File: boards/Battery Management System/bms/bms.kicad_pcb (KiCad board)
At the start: 2 copper layers, 23 parts, among them J1 Screw_Terminal_01x05, J2 Screw_Terminal_01x02, J3 Screw_Terminal_01x02, Q1 PMOS, Q2 PMOS, Q3 PMOS, Q4 PMOS, Q5 NMOS, Q6 NMOS, Q7 NMOS, Q8 NMOS, U1 BD48L32G, U2 BD48L32G, U3 BD48L32G, U4 BD48L32G

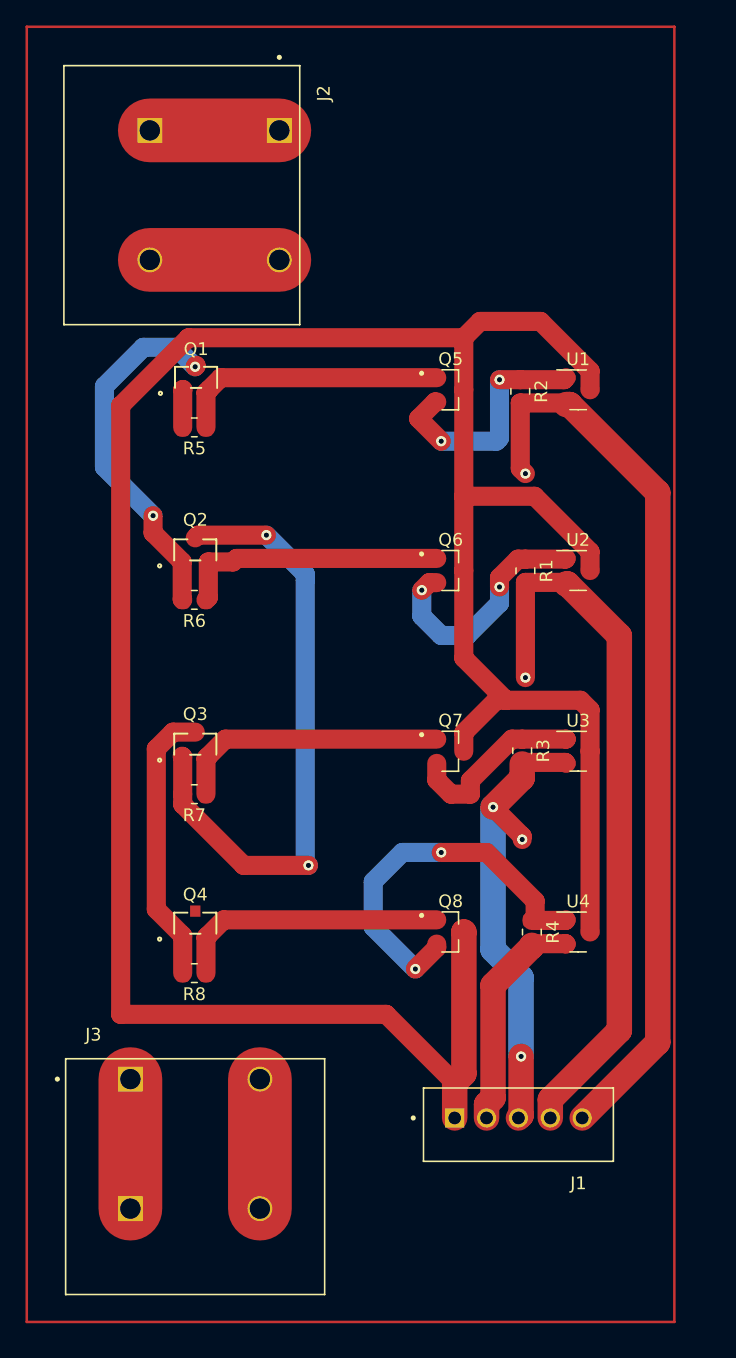
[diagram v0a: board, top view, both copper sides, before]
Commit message: updated bms schematic and layout
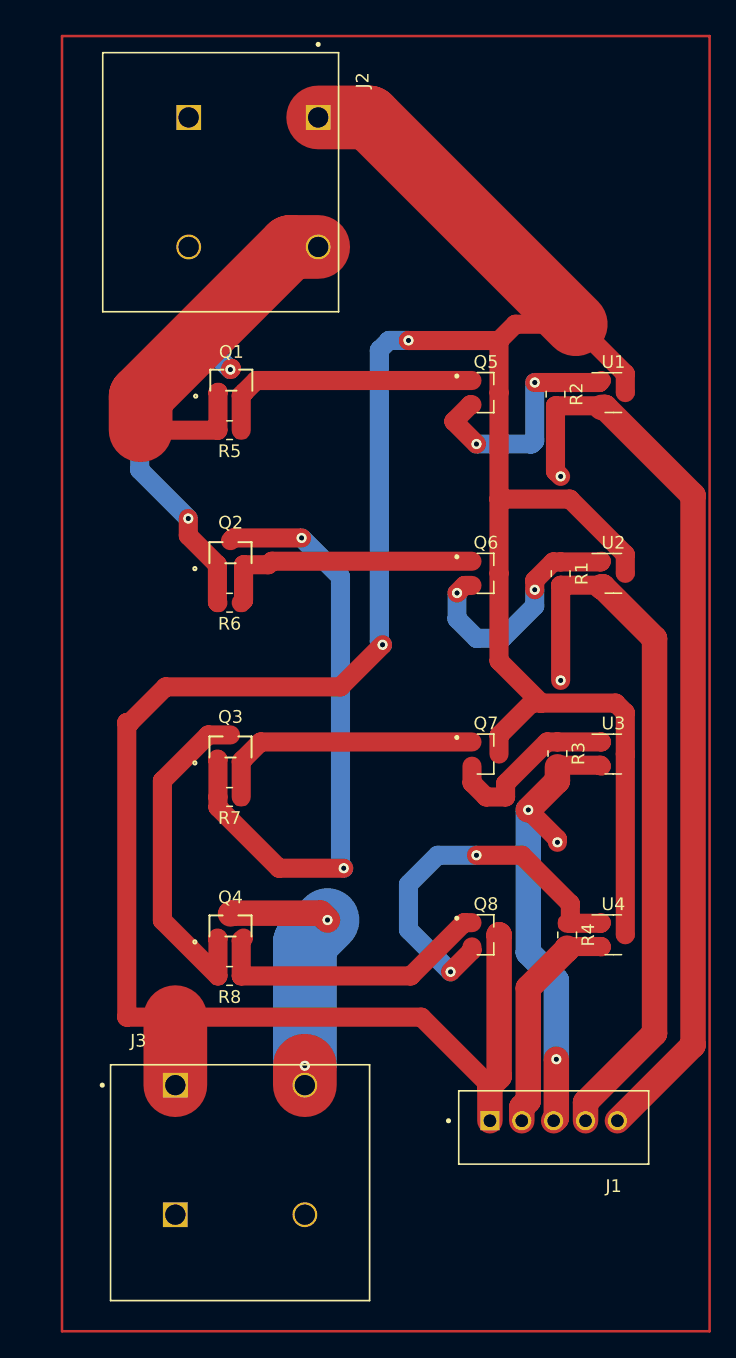
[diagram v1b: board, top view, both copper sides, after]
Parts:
- J2, J3: value Screw_Terminal_01x02 -> 1986660-2
- moved J3 3.56 mm to (102.6, 119.9)
- moved J2 3.21 mm to (113.8, 43.9)
- moved J1 2.77 mm to (132.3, 123.2)
- moved Q1 2.77 mm to (107.0, 64.6)
- moved R1 2.77 mm to (132.8, 79.7)
- moved R2 2.77 mm to (132.4, 65.6)
- moved R5 2.77 mm to (106.8, 68.5)
- moved R6 2.77 mm to (106.8, 82.0)
- moved R7 2.77 mm to (106.8, 97.2)
- moved R8 2.77 mm to (106.8, 111.3)
- moved U1 2.77 mm to (136.9, 65.5)
- moved U2 2.77 mm to (136.9, 79.7)
- moved U3 2.77 mm to (136.9, 93.9)
- moved U4 2.77 mm to (136.9, 108.1)
- moved Q2 2.77 mm to (106.9, 78.1)
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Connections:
- J2 pad 1_1: (no net) -> GND
- J2 pad 2_1: (no net) -> /V_BAT_IN
- J3 pad 1_1: (no net) -> GND
- J3 pad 2_1: (no net) -> /V_BAT_OUT
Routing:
- net (no net): track 40.6 -> 0.00 mm
- net GND: track 206.9 -> 243.2 mm, vias 0 -> 2
- net /V_BAT_IN: track 3.09 -> 30.7 mm
- net /V_BAT_OUT: track 0.00 -> 21.5 mm, vias 0 -> 2
- net Net-(Q3-S): track 22.1 -> 27.0 mm
- net Net-(Q4-G): track 21.7 -> 23.2 mm

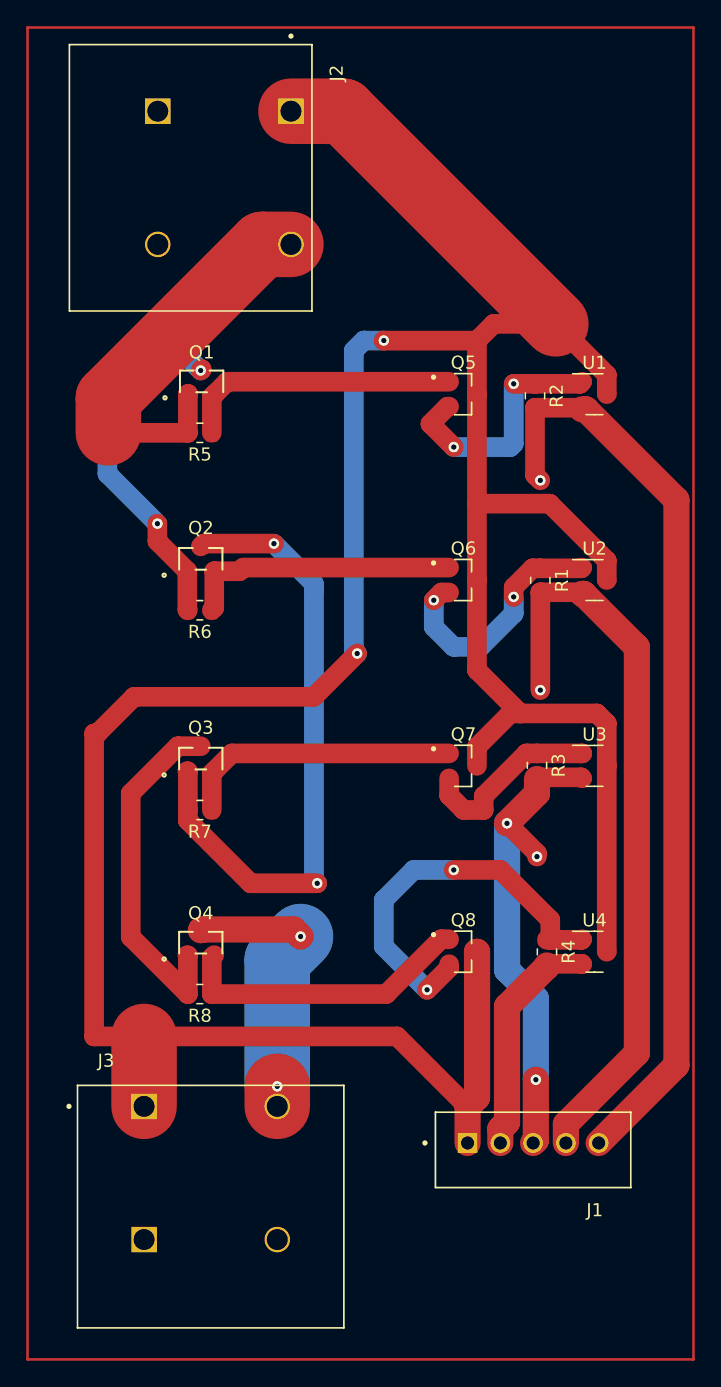
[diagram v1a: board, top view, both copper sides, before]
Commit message: Redid pcb layout and added LEDs.
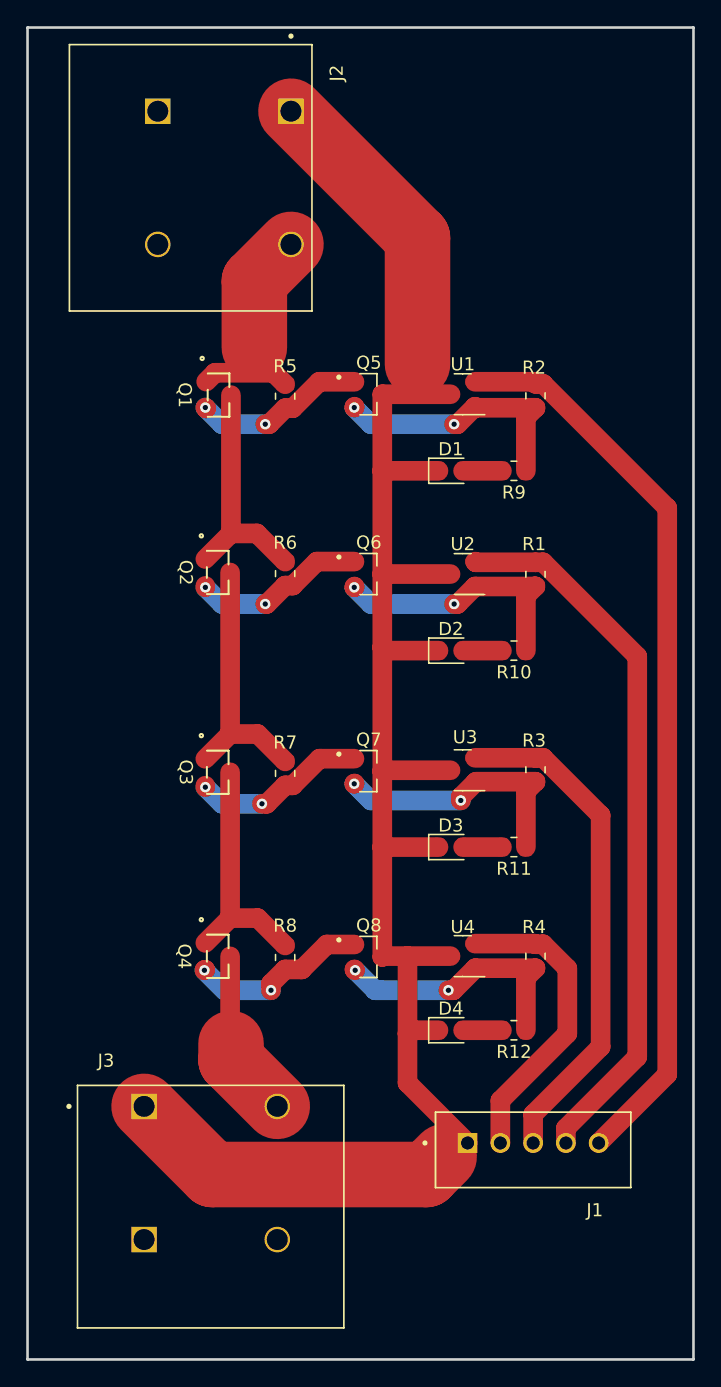
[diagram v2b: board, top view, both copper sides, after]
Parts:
- added D1: LED, LED_SMD:LED_0805_2012Metric, F.Cu at (126.0, 71.4)
- added D2: LED, LED_SMD:LED_0805_2012Metric, F.Cu at (126.0, 85.1)
- added D3: LED, LED_SMD:LED_0805_2012Metric, F.Cu at (126.0, 100.1)
- added D4: LED, LED_SMD:LED_0805_2012Metric, F.Cu at (126.0, 114.0)
- added R10: 6Ω, Resistor_SMD:R_0805_2012Metric, F.Cu at (130.8, 85.1)
- added R11: 6Ω, Resistor_SMD:R_0805_2012Metric, F.Cu at (130.8, 100.1)
- added R12: 6Ω, Resistor_SMD:R_0805_2012Metric, F.Cu at (130.8, 114.0)
- added R9: 6Ω, Resistor_SMD:R_0805_2012Metric, F.Cu at (130.8, 71.4)
- moved U2 10.1 mm to (126.9, 79.2), turned to 180 degrees
- moved U3 10.1 mm to (126.9, 94.2), turned to 180 degrees
- moved U4 10.1 mm to (126.9, 108.4), turned to 180 degrees
- moved U1 10.1 mm to (126.9, 65.5), turned to 180 degrees
- moved Q6 7.23 mm to (119.7, 79.2)
- moved Q7 7.23 mm to (119.7, 94.3)
- moved Q8 7.23 mm to (119.7, 108.5)
- moved Q5 7.22 mm to (119.7, 65.5)
- moved R7 7.08 mm to (113.3, 94.5), turned to 90 degrees
- moved R8 7.08 mm to (113.3, 108.5), turned to 90 degrees
- moved R5 7.08 mm to (113.3, 65.7), turned to 90 degrees
- moved R6 7.08 mm to (113.3, 79.2), turned to 90 degrees
- moved Q1 1.66 mm to (108.3, 65.6), turned to -90 degrees
- moved Q2 1.66 mm to (108.2, 79.1), turned to -90 degrees
- moved Q3 1.66 mm to (108.2, 94.4), turned to -90 degrees
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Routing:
- net GND: track 243.2 -> 144.3 mm, vias 2 -> 0
- net Net-(Q2-S): track 48.6 -> 20.1 mm, vias 2 -> 0
- net /V_BAT_IN: track 30.7 -> 15.7 mm
- net /CON_4: track 30.3 -> 20.2 mm
- net Net-(Q1-S): track 28.5 -> 18.3 mm, vias 2 -> 0
- net Net-(Q4-G): track 23.2 -> 13.9 mm, vias 0 -> 2
- net /V_BAT_OUT: track 21.5 -> 12.9 mm, vias 2 -> 0
- net Net-(Q3-G): track 21.8 -> 13.4 mm, vias 0 -> 2
- net Net-(Q1-G): track 21.7 -> 13.3 mm, vias 0 -> 2
- net Net-(Q3-S): track 27.0 -> 18.9 mm
- net Net-(Q2-G): track 21.1 -> 13.4 mm, vias 0 -> 2
- net /CON_3: track 14.3 -> 20.4 mm, vias 0 -> 2
- net /V_CELL_4: track 17.7 -> 23.3 mm
- net Net-(D4-A): track 0.00 -> 2.96 mm
- net Net-(D3-A): track 0.00 -> 2.96 mm
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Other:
- board outline added: 50.8 x 101.6 mm

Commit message: Worked on schematic and PCB
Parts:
- removed Q1, Q2, Q3, Q4: PMOS, BSS84_7_F:SOT-23_DIO
- removed Q5, Q6, Q7, Q8: NMOS, BSS138:SOT95P240X111-3N
- added K1: HE1AN-W-DC6V-Y6, footprints:HE1AN-W-DC6V_PAN, F.Cu at (163.2, 70.5)
- added K2: HE1AN-W-DC6V-Y6, footprints:HE1AN-W-DC6V_PAN, F.Cu at (200.0, 70.5)
- added K3: HE1AN-W-DC6V-Y6, footprints:HE1AN-W-DC6V_PAN, F.Cu at (236.9, 70.5)
- added K4: HE1AN-W-DC6V-Y6, footprints:HE1AN-W-DC6V_PAN, F.Cu at (273.7, 70.5)
- added R13: 100kΩ, Resistor_SMD:R_0805_2012Metric, F.Cu at (61.4, 82.6)
- added R14: 100kΩ, Resistor_SMD:R_0805_2012Metric, F.Cu at (61.4, 88.5)
- added R15: 100kΩ, Resistor_SMD:R_0805_2012Metric, F.Cu at (61.4, 94.0)
- added R16: 100kΩ, Resistor_SMD:R_0805_2012Metric, F.Cu at (61.4, 96.9)
- added R17: 5kΩ, Resistor_SMD:R_0805_2012Metric, F.Cu at (65.8, 82.6)
- added R18: 10kΩ, Resistor_SMD:R_0805_2012Metric, F.Cu at (65.8, 88.5)
- added R19: 10kΩ, Resistor_SMD:R_0805_2012Metric, F.Cu at (65.8, 94.0)
- added R20: 5kΩ, Resistor_SMD:R_0805_2012Metric, F.Cu at (65.8, 96.9)
- added R21: 10kΩ, Resistor_SMD:R_0805_2012Metric, F.Cu at (70.2, 82.6)
- added R22: 5kΩ, Resistor_SMD:R_0805_2012Metric, F.Cu at (70.2, 88.5)
- added R23: 10kΩ, Resistor_SMD:R_0805_2012Metric, F.Cu at (70.2, 94.0)
- added R24: 5kΩ, Resistor_SMD:R_0805_2012Metric, F.Cu at (70.2, 96.9)
- added U5: Opamp_Quad, footprints:SOT23_DYY_TEX, F.Cu at (62.0, 101.4)
- R10, R11, R12, R9: value 6Ω -> 70Ω
- moved R5 57.1 mm to (157.6, 101.8), turned to 0 degrees
- moved R6 51.1 mm to (157.6, 104.8), turned to 0 degrees
- moved R7 46.2 mm to (157.6, 107.7), turned to 0 degrees
- moved R8 44.3 mm to (157.6, 110.7), turned to 0 degrees
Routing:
- net GND: track 144.3 -> 121.0 mm
- net Net-(Q2-S): track 20.1 -> 0.00 mm
- net Net-(Q3-S): track 18.9 -> 0.00 mm
- net Net-(Q1-S): track 18.3 -> 0.00 mm
- net /V_BAT_IN: track 15.7 -> 0.00 mm
- net Net-(Q4-G): track 13.9 -> 0.00 mm, vias 2 -> 0
- net Net-(Q3-G): track 13.4 -> 0.00 mm, vias 2 -> 0
- net Net-(Q2-G): track 13.4 -> 0.00 mm, vias 2 -> 0
- net Net-(Q1-G): track 13.3 -> 0.00 mm, vias 2 -> 0
- net /V_BAT_OUT: track 12.9 -> 0.00 mm
- net /CON_3: track 20.4 -> 11.7 mm, vias 2 -> 1
- net /CON_2: track 20.2 -> 12.0 mm, vias 2 -> 1
- net /CON_1: track 20.1 -> 11.9 mm, vias 2 -> 1
- net /CON_4: track 20.2 -> 12.4 mm, vias 2 -> 1

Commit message: Edited schematic and PCB
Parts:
- added U5: Opamp_Quad, footprints:SOT23_DBV_5_TEX-L, F.Cu at (48.9, 133.1)
- added U6: 74AUC2G08, footprints:D14-L, F.Cu at (50.4, 125.7)
- added U7: 74AUC2G08, footprints:D14-L, F.Cu at (58.5, 125.7)
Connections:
- K1 pad 1: Net-(K1-Pad1) -> /V_BAT_OUT

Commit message: Edited schematic and PCB
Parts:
- removed K2, K3, K4: HE1AN-W-DC6V-Y6, footprints:HE1AN-W-DC6V_PAN
- removed the R7 at (157.6, 107.7)
- removed the R8 at (157.6, 110.7)
- removed the U5 at (62.0, 101.4)
- removed the U5 at (48.9, 133.1)
- removed U7: 74AUC2G08, footprints:D14-L
- added U5: SN74HC08DR, SN74HC08DR:SOIC127P600X175-14N, F.Cu at (25.5, 108.0)
- K1: footprint footprints:HE1AN-W-DC6V_PAN -> HE1AN_W_DC6V_Y6:HE1AN-W-DC6V_PAN
- R5: value 100kΩ -> 10kΩ
- R6: value 100kΩ -> 5kΩ
- U6: value 74AUC2G08 -> TL071HIDBVR; footprint footprints:D14-L -> TL071HIDBVR:SOT23_DBV_5_TEX-L
- moved R5 103.1 mm to (62.6, 61.7)
- moved R6 103.1 mm to (62.6, 64.7)
- moved U6 65.4 mm to (67.3, 62.5)
- renumbered R2 to R1, R12 to R10, R1 to R2, R9 to R7, R10 to R8, R11 to R9
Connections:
- K1 pad 5: Net-(K1-Pad5) -> Net-(U6-OUT)
- R5 pad 1: Net-(Q1-G) -> GND
- R5 pad 2: /V_BAT_IN -> Net-(U6-IN-)
- R6 pad 1: Net-(Q2-G) -> Net-(U6-IN-)
- R6 pad 2: Net-(Q1-S) -> Net-(U6-OUT)
- U6 pad 1: /CON_1 -> Net-(U6-OUT)
- U6 pad 2: /CON_2 -> GND
- U6 pad 4: (no net) -> Net-(U6-IN-)
- U6 pad 5: Net-(U6-Pad5) -> /V_BAT_IN

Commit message: Updated Schematic and PCB
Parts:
- removed R14, R15, R16: 100kΩ, Resistor_SMD:R_0805_2012Metric
- removed R17, R20, R22, R24: 5kΩ, Resistor_SMD:R_0805_2012Metric
- removed R18, R19, R21, R23: 10kΩ, Resistor_SMD:R_0805_2012Metric
- moved U5 100.3 mm to (117.6, 68.3), turned to 180 degrees
- moved R11 74.6 mm to (127.3, 47.5), turned to -90 degrees
- moved R6 73.3 mm to (133.9, 47.5), turned to 90 degrees
- moved R5 71.7 mm to (133.9, 53.8), turned to 90 degrees
- moved U6 59.6 mm to (126.2, 53.8)
- moved K1 54.1 mm to (122.7, 106.4), turned to 180 degrees
- moved D1 7.76 mm to (132.4, 67.0)
- moved D2 7.76 mm to (132.4, 80.7)
- moved D3 7.76 mm to (132.4, 95.7)
- moved D4 7.76 mm to (132.4, 109.7)
- moved R10 7.76 mm to (137.2, 109.7)
- moved R2 7.76 mm to (138.8, 74.9)
- moved R3 7.76 mm to (138.8, 89.8)
- moved R4 7.76 mm to (138.8, 104.0)
- moved R7 7.76 mm to (137.2, 67.0)
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- renumbered R13 to R11
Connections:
- U5 pad 1: /CON_1 -> /CON_4
- U5 pad 10: Net-(U5-2Y) -> Net-(U5-1Y)
- U5 pad 2: /CON_2 -> /CON_3
- U5 pad 4: /CON_3 -> /CON_2
- U5 pad 5: /CON_4 -> /CON_1
- U5 pad 9: Net-(U5-1Y) -> Net-(U5-2Y)
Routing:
- net /V_BAT_IN: track 0.00 -> 61.8 mm
- net GND: track 121.0 -> 171.9 mm, vias 0 -> 3
- net Net-(U6-OUT): track 0.00 -> 50.9 mm, vias 0 -> 3
- net /CON_4: track 12.4 -> 54.1 mm, vias 1 -> 2
- net /CON_3: track 11.7 -> 41.8 mm, vias 1 -> 2
- net /CON_2: track 12.0 -> 28.6 mm, vias 1 -> 2
- net /V_BAT_OUT: track 0.00 -> 16.5 mm
- net /CON_1: track 11.9 -> 26.3 mm, vias 1 -> 2
- net Net-(U5-3Y): track 0.00 -> 13.9 mm
- net Net-(U6-IN-): track 0.00 -> 12.6 mm, vias 0 -> 2
- net /V_CELL_4: track 23.3 -> 34.1 mm, vias 0 -> 2
- net /V_CELL_2: track 54.7 -> 61.5 mm, vias 0 -> 2
- net Net-(U5-1Y): track 0.00 -> 6.45 mm
- net /V_CELL_3: track 38.5 -> 44.6 mm
- net Net-(U5-2Y): track 0.00 -> 4.95 mm
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
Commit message: Updated pcb
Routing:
- net GND: track 171.9 -> 2.60 mm, vias 3 -> 1
- net /CON_1: track 26.3 -> 27.4 mm
- net /CON_2: track 28.6 -> 29.3 mm

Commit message: Updated pcb
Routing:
- net Net-(U6-OUT): track 50.9 -> 2.31 mm, vias 3 -> 1
- net GND: track 2.60 -> 0.00 mm, vias 1 -> 0
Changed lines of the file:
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@@
   (segment (start 141.224 105.486001) (end 138.841998 103.103999) (width 1.5) (layer "B.Cu") (net 3))
   (segment (start 129.794 119.38) (end 133.35 119.38) (width 1.5) (layer "B.Cu") (net 3))
-  (segment (start 124.97435 53.848) (end 125.8617 53.848) (width 0.5) (layer "F.Cu") (net 4))
-  (segment (start 125.8617 53.848) (end 126.287923 54.274223) (width 0.5) (layer "F.Cu") (net 4))
-  (segment (start 126.287923 54.274223) (end 126.287923 55.387432) (width 0.5) (layer "F.Cu") (net 4))
-  (via (at 126.287923 55.387432) (size 0.8) (drill 0.4) (layers "F.Cu" "B.Cu") (net 4))
   (segment (start 137.264 122.6485) (end 143.51 116.4025) (width 1.5) (layer "F.Cu") (net 5))
   (segment (start 140.365998 60.355998) (end 138.841998 60.355998) (width 1.5) (layer "F.Cu") (net 5))
@@
   (segment (start 143.51 63.5) (end 140.365998 60.355998) (width 1.5) (layer "F.Cu") (net 5))
   (segment (start 134.230999 60.198) (end 138.684 60.198) (width 1.5) (layer "F.Cu") (net 5))
-  (segment (start 109.22 58.674) (end 109.22 71.882) (width 5) (layer "F.Cu") (net 6))
   (segment (start 127.254 48.4105) (end 127.254 49.022) (width 1.5) (layer "F.Cu") (net 6))
   (segment (start 115.127 73.725) (end 115.316 73.914) (width 1) (layer "F.Cu") (net 6))
   (segment (start 127.254 52.650349) (end 127.50165 52.897999) (width 1.5) (layer "F.Cu") (net 6))
+  (segment (start 113.792 54.102) (end 109.22 58.674) (width 5) (layer "F.Cu") (net 6))
   (segment (start 115.316 81.559999) (end 120.182 86.425999) (width 5) (layer "F.Cu") (net 6))
-  (segment (start 113.792 54.102) (end 109.22 58.674) (width 5) (layer "F.Cu") (net 6))
+  (segment (start 109.22 58.674) (end 109.22 71.882) (width 5) (layer "F.Cu") (net 6))
   (segment (start 127.254 49.022) (end 127.254 52.650349) (width 1.5) (layer "F.Cu") (net 6))
   (segment (start 115.316 73.914) (end 115.316 77.978) (width 5) (layer "F.Cu") (net 6))
   (segment (start 115.316 77.978) (end 115.316 81.559999) (width 5) (layer "F.Cu") (net 6))
   (segment (start 118.364 49.53) (end 124.46 49.53) (width 5) (layer "F.Cu") (net 6))
+  (segment (start 109.22 71.882) (end 115.316 77.978) (width 5) (layer "F.Cu") (net 6))
   (segment (start 113.792 54.102) (end 118.364 49.53) (width 5) (layer "F.Cu") (net 6))
-  (segment (start 109.22 71.882) (end 115.316 77.978) (width 5) (layer "F.Cu") (net 6))
   (segment (start 115.127 72.136) (end 115.127 73.725) (width 1) (layer "F.Cu") (net 6))
   (segment (start 112.746 119.8545) (end 112.746 113.862) (width 5) (layer "F.Cu") (net 7))
@@
   (segment (start 136.283998 95.692) (end 133.319498 95.692) (width 1.5) (layer "F.Cu") (net 14))
   (segment (start 133.319498 109.662) (end 136.283998 109.662) (width 1.5) (layer "F.Cu") (net 15))
-  (segment (start 132.08 46.736) (end 133.7075 46.736) (width 1) (layer "F.Cu") (net 16))
-  (segment (start 124.97435 52.897999) (end 123.908401 52.897999) (width 1) (layer "F.Cu") (net 16))
-  (segment (start 104.14 73.152) (end 99.958895 77.333105) (width 5) (layer "F.Cu") (net 16))
-  (segment (start 99.958895 77.333105) (end 99.107381 77.333105) (width 5) (layer "F.Cu") (net 16))
+  (segment (start 133.858 46.5855) (end 131.9765 46.5855) (width 1) (layer "F.Cu") (net 16))
   (segment (start 133.7075 46.736) (end 133.858 46.5855) (width 1) (layer "F.Cu") (net 16))
-  (segment (start 123.698 53.1084) (end 123.698 53.594) (width 1) (layer "F.Cu") (net 16))
-  (segment (start 123.908401 52.897999) (end 123.698 53.1084) (width 1) (layer "F.Cu") (net 16))
-  (via (at 132.08 46.736) (size 0.8) (drill 0.4) (layers "F.Cu" "B.Cu") (net 16))
-  (via (at 123.698 53.594) (size 0.8) (drill 0.4) (layers "F.Cu" "B.Cu") (net 16))
-  (via (at 104.14 73.152) (size 0.8) (drill 0.4) (layers "F.Cu" "B.Cu") (net 16))
-  (segment (start 130.556 46.736) (end 125.476 51.816) (width 5) (layer "B.Cu") (net 16))
-  (segment (start 123.698 53.594) (end 104.14 73.152) (width 5) (layer "B.Cu") (net 16))
-  (segment (start 132.08 46.736) (end 130.556 46.736) (width 5) (layer "B.Cu") (net 16))
-  (segment (start 125.476 51.816) (end 127 51.816) (width 1) (layer "B.Cu") (net 16))
-  (segment (start 125.476 51.816) (end 123.698 53.594) (width 5) (layer "B.Cu") (net 16))
+  (segment (start 131.9765 46.5855) (end 131.826 46.736) (width 1) (layer "F.Cu") (net 16))
+  (via (at 131.826 46.736) (size 0.8) (drill 0.4) (layers "F.Cu" "B.Cu") (net 16))
   (segment (start 133.858 52.9355) (end 133.858 50.8) (width 1.5) (layer "F.Cu") (net 17))
   (segment (start 127.50165 54.798001) (end 128.966001 54.798001) (width 1.5) (layer "F.Cu") (net 17))
